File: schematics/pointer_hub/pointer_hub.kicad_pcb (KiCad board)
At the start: 2 copper layers, 34 parts, among them J3 Conn_02x25_Counter_Clockwise, U1 74HC193, U10 74HC245, U11 74HC193, U12 74HC193, U13 74HC193, U14 74HC193, U2 74HC193, U3 74HC193, U4 74HC245, U5 74HC193, U6 74HC245, U7 74HC00, U8 74HC245, U9 74HC00

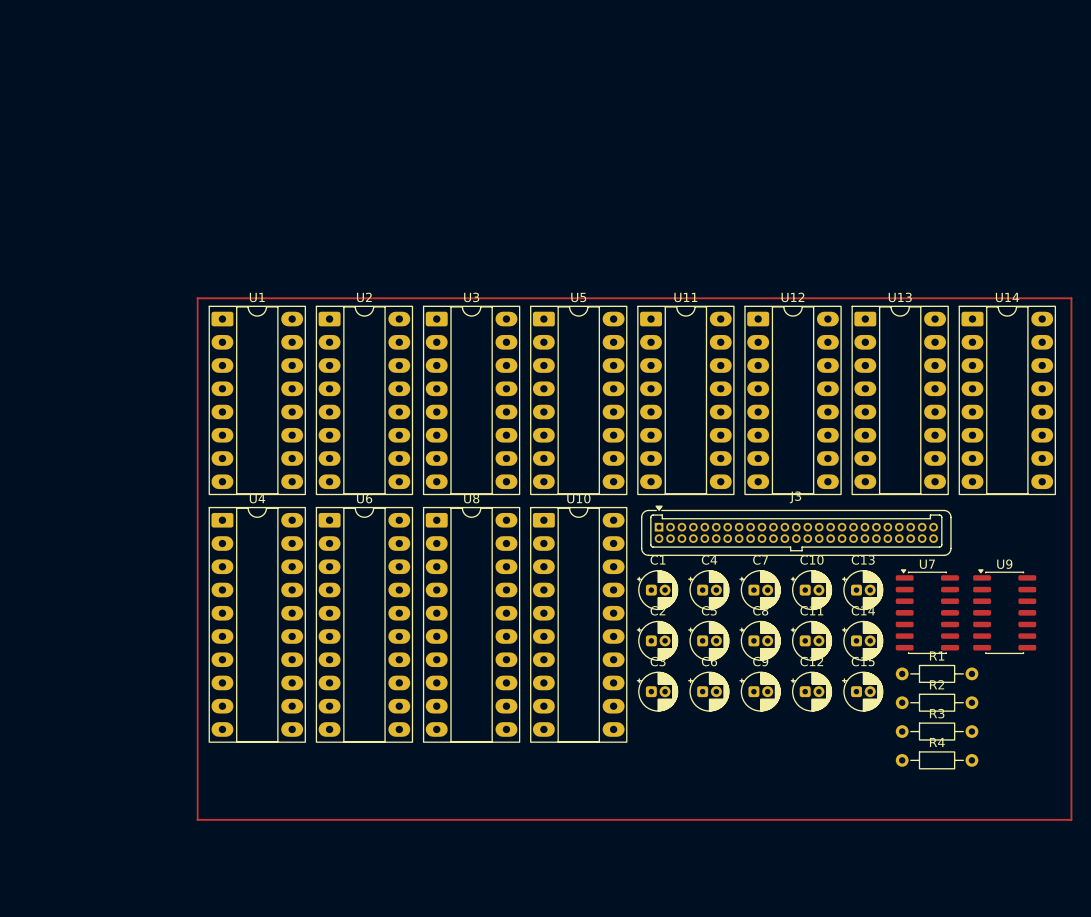
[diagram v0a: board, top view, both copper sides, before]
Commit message: added lowarg to pointerhub, also replaced resistor + vcc logic by grnd and changing A and B pins(A was in became out...)
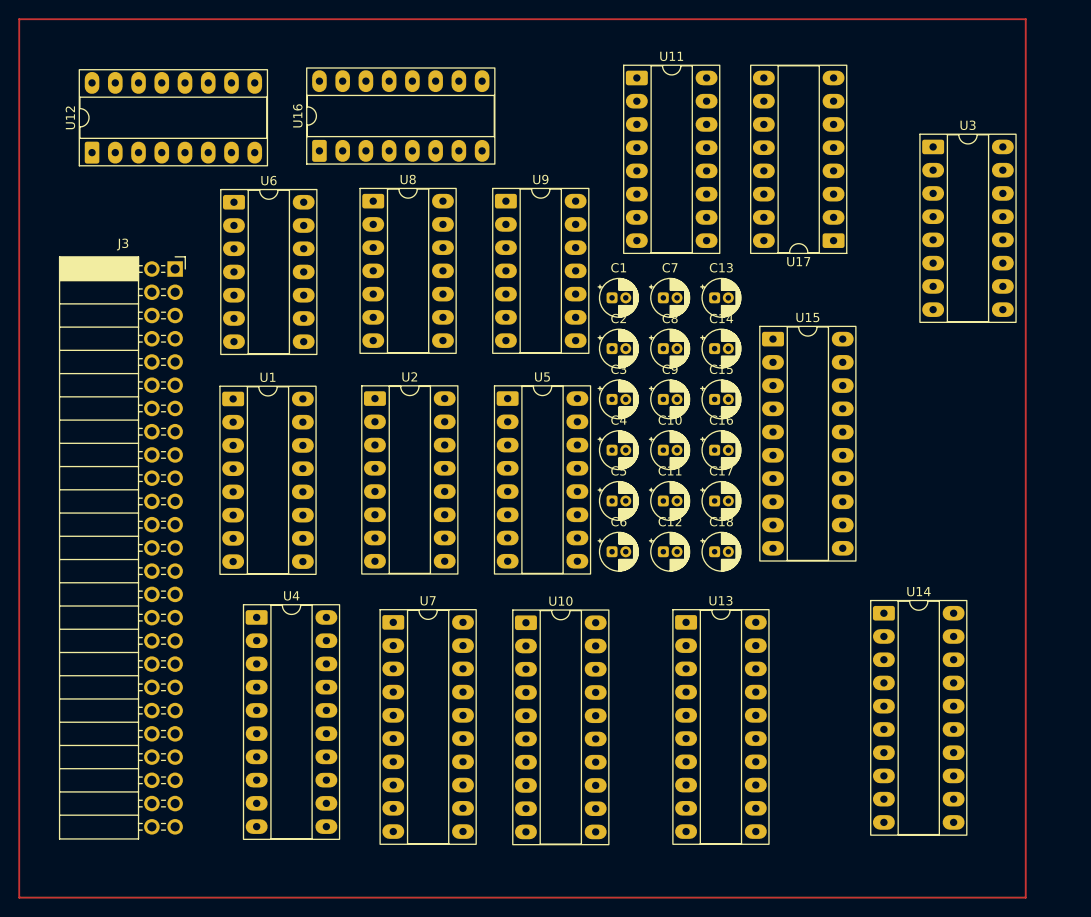
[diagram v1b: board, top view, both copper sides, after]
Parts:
- removed R1, R2, R3, R4: R, Resistor_THT:R_Axial_DIN0204_L3.6mm_D1.6mm_P7.62mm_Horizontal
- added C16: C, Capacitor_THT:CP_Radial_D4.0mm_P1.50mm, F.Cu at (149.5, 86.6)
- added C17: C, Capacitor_THT:CP_Radial_D4.0mm_P1.50mm, F.Cu at (149.5, 92.2)
- added C18: C, Capacitor_THT:CP_Radial_D4.0mm_P1.50mm, F.Cu at (149.5, 97.7)
- added U15: 74LS245, Package_DIP:DIP-20_W7.62mm_Socket_LongPads, F.Cu at (155.9, 74.5)
- added U16: 74LS193, Package_DIP:DIP-16_W7.62mm_Socket_LongPads, F.Cu at (106.3, 53.9)
- added U17: 74LS193, Package_DIP:DIP-16_W7.62mm_Socket_LongPads, F.Cu at (162.5, 63.7)
- J3: footprint Connector_Harwin:Harwin_Gecko-G125-FVX5005L0X_2x25_P1.25mm_Vertical -> Connector_PinSocket_2.54mm:PinSocket_2x25_P2.54mm_Horizontal
- U1, U11, U12, U2, U3, U5: value 74HC193 -> 74LS193
- U10, U4: value 74HC245 -> 74LS245
- U13, U14: value 74HC193 -> 74LS245; footprint Package_DIP:DIP-16_W7.62mm_Socket_LongPads -> Package_DIP:DIP-20_W7.62mm_Socket_LongPads
- U6, U8: value 74HC245 -> 74LS00; footprint Package_DIP:DIP-20_W7.62mm_Socket_LongPads -> Package_DIP:DIP-14_W7.62mm_Socket_LongPads
- U7: value 74HC00 -> 74LS574; footprint Package_SO:SOIC-14_3.9x8.7mm_P1.27mm -> Package_DIP:DIP-20_W7.62mm_Socket_LongPads
- U9: value 74HC00 -> 74LS08; footprint Package_SO:SOIC-14_3.9x8.7mm_P1.27mm -> Package_DIP:DIP-14_W7.62mm_Socket_LongPads
- moved U12 75.0 mm to (81.5, 54.1), turned to 90 degrees
- moved U9 70.7 mm to (126.7, 59.4)
- moved J3 59.9 mm to (90.5, 66.8)
- moved U7 58.4 mm to (114.4, 105.4)
- moved U3 57.4 mm to (173.4, 53.5)
- moved U13 38.5 mm to (146.4, 105.4)
- moved U6 36.3 mm to (97.0, 59.5)
- moved U8 35.6 mm to (112.2, 59.4)
- moved C13 35.5 mm to (149.5, 70.0)
- moved C14 35.5 mm to (149.5, 75.5)
- moved C15 35.5 mm to (149.5, 81.0)
- moved U14 33.6 mm to (168.0, 104.4)
- moved C7 33.4 mm to (143.9, 70.0)
- moved C8 33.4 mm to (143.9, 75.5)
- moved C9 33.4 mm to (143.9, 81.0)
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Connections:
- C1 pad 1: +5V -> GND
- C1 pad 2: GND -> VCC
- C10 pad 1: +5V -> GND
- C10 pad 2: GND -> VCC
- C11 pad 1: +5V -> GND
- C11 pad 2: GND -> VCC
- C12 pad 1: +5V -> GND
- C12 pad 2: GND -> VCC
- C13 pad 1: +5V -> GND
- C13 pad 2: GND -> VCC
- C14 pad 1: +5V -> GND
- C14 pad 2: GND -> VCC
- C15 pad 2: +5V -> VCC
- C2 pad 1: +5V -> GND
- C2 pad 2: GND -> VCC
- C3 pad 1: +5V -> GND
- C3 pad 2: GND -> VCC
- C4 pad 1: +5V -> GND
- C4 pad 2: GND -> VCC
- C5 pad 1: +5V -> VCC
- C6 pad 1: +5V -> VCC
- C7 pad 1: +5V -> GND
- C7 pad 2: GND -> VCC
- C8 pad 1: +5V -> VCC
- C9 pad 1: +5V -> GND
- C9 pad 2: GND -> VCC
- J3 pad 1: GND -> VCC
- J3 pad 10: /BUS6 -> unconnected-(J3-Pin_10-Pad10)
- J3 pad 11: /BUS7 -> /BUS0
- J3 pad 12: /SPReset -> /BUS1
- J3 pad 13: /SPInc -> /BUS2
- J3 pad 14: /SPDec -> /BUS3
- J3 pad 15: /SPHighIn -> /BUS4
- J3 pad 16: /SPLowIn -> /BUS5
- J3 pad 17: /~SPLowOut -> /BUS6
- J3 pad 18: /~SPHighOut -> /BUS7
- J3 pad 19: unconnected-(J3-Pin_19-Pad19) -> GND
- J3 pad 2: /CLK -> GND
- J3 pad 25: unconnected-(J3-Pin_25-Pad25) -> VCC
- J3 pad 26: unconnected-(J3-Pin_26-Pad26) -> VCC
- J3 pad 3: GND -> /~{Clk}
- J3 pad 33: /~PСHighOut -> /~{PСHighOut}
- J3 pad 34: /~PСLowOut -> /~{PСLowOut}
- J3 pad 39: /PCReset -> /Reset
- J3 pad 4: /BUS0 -> /Clk
- J3 pad 40: unconnected-(J3-Pin_40-Pad40) -> /SPInc
- J3 pad 41: unconnected-(J3-Pin_41-Pad41) -> /SPDec
- J3 pad 42: unconnected-(J3-Pin_42-Pad42) -> /SPHighIn
- J3 pad 43: unconnected-(J3-Pin_43-Pad43) -> /SPLowIn
- J3 pad 44: unconnected-(J3-Pin_44-Pad44) -> /~{SPLowOut}
- J3 pad 45: unconnected-(J3-Pin_45-Pad45) -> /~{SPHighOut}
- J3 pad 47: /PULSE -> unconnected-(J3-Pin_47-Pad47)
- J3 pad 48: GND -> /PULSE
- J3 pad 49: /~CLK -> GND
- J3 pad 5: /BUS1 -> /LFromD
- J3 pad 50: GND -> VCC
- J3 pad 6: /BUS2 -> /~{LToD}
- J3 pad 7: /BUS3 -> unconnected-(J3-Pin_7-Pad7)
- J3 pad 8: /BUS4 -> unconnected-(J3-Pin_8-Pad8)
- J3 pad 9: /BUS5 -> unconnected-(J3-Pin_9-Pad9)
- U1 pad 1: /BUS1 -> /BUS5
- U1 pad 10: /BUS2 -> /BUS6
- U1 pad 11: /Pl_A -> /Ph_B
- U1 pad 14: /PCReset -> /Reset
- U1 pad 15: /BUS0 -> /BUS4
- U1 pad 16: +5V -> VCC
- U1 pad 2: /DL_A1 -> /DH_B5
- U1 pad 3: /DL_A0 -> /DH_B4
- U1 pad 6: /DL_A2 -> /DH_B6
- U1 pad 7: /DL_A3 -> /DH_B7
- U1 pad 9: /BUS3 -> /BUS7
- U10 pad 1: Net-(U10-A->B) -> GND
- U10 pad 11: /BUS7 -> /DH_B7
- U10 pad 12: /BUS6 -> /DH_B6
- U10 pad 13: /BUS5 -> /DH_B5
- U10 pad 14: /BUS4 -> /DH_B4
- U10 pad 15: /BUS3 -> /DH_B3
- U10 pad 16: /BUS2 -> /DH_B2
- U10 pad 17: /BUS1 -> /DH_B1
- U10 pad 18: /BUS0 -> /DH_B0
- U10 pad 19: /~SPLowOut -> /~{SPHighOut}
- U10 pad 2: /DL_B0 -> /BUS0
- U10 pad 20: +5V -> VCC
- U10 pad 3: /DL_B1 -> /BUS1
- U10 pad 4: /DL_B2 -> /BUS2
- U10 pad 5: /DL_B3 -> /BUS3
- U10 pad 6: /DL_B4 -> /BUS4
- U10 pad 7: /DL_B5 -> /BUS5
- U10 pad 8: /DL_B6 -> /BUS6
- U10 pad 9: /DL_B7 -> /BUS7
- U11 pad 11: /Ph_B -> /Pl_B
- U11 pad 14: /SPReset -> /Reset
- U11 pad 16: +5V -> VCC
- U11 pad 2: /DH_B5 -> /DL_B5
- U11 pad 3: /DH_B4 -> /DL_B4
- U11 pad 4: Net-(U11-DOWN) -> /CPd_B
- U11 pad 5: Net-(U11-UP) -> /CPu_B
- U11 pad 6: /DH_B6 -> /DL_B6
- U11 pad 7: /DH_B7 -> /DL_B7
- U12 pad 11: /Ph_B -> /Pl_B
- U12 pad 12: unconnected-(U12-~{CO}-Pad12) -> Net-(U1-UP)
- U12 pad 13: unconnected-(U12-~{BO}-Pad13) -> Net-(U1-DOWN)
- U12 pad 14: /SPReset -> /Reset
- U12 pad 16: +5V -> VCC
- U12 pad 2: /DH_B1 -> /DL_B1
- U12 pad 3: /DH_B0 -> /DL_B0
- U12 pad 6: /DH_B2 -> /DL_B2
- U12 pad 7: /DH_B3 -> /DL_B3
- U13 pad 1: /BUS5 -> GND
- U13 pad 10: /BUS6 -> GND
- U13 pad 11: /Pl_B -> Net-(U13-B7)
- U13 pad 12: Net-(U13-~{CO}) -> Net-(U13-B6)
- U13 pad 13: Net-(U13-~{BO}) -> Net-(U13-B5)
- U13 pad 14: /SPReset -> Net-(U13-B4)
- U13 pad 15: /BUS4 -> Net-(U13-B3)
- U13 pad 16: +5V -> Net-(U13-B2)
- U13 pad 2: /DL_B5 -> /BUS0
- U13 pad 3: /DL_B4 -> /BUS1
- U13 pad 4: /CPd_B -> /BUS2
- U13 pad 5: /CPu_B -> /BUS3
- U13 pad 6: /DL_B6 -> /BUS4
- U13 pad 7: /DL_B7 -> /BUS5
- U13 pad 8: GND -> /BUS6
- U14 pad 1: /BUS1 -> GND
- U14 pad 10: /BUS2 -> GND
- U14 pad 11: /Pl_B -> /DL_A7
- U14 pad 12: Net-(U11-UP) -> /DL_A6
- U14 pad 13: Net-(U11-DOWN) -> /DL_A5
- U14 pad 14: /SPReset -> /DL_A4
- U14 pad 15: /BUS0 -> /DL_A3
- U14 pad 16: +5V -> /DL_A2
- U14 pad 2: /DL_B1 -> /BUS0
- U14 pad 3: /DL_B0 -> /BUS1
- U14 pad 4: Net-(U13-~{BO}) -> /BUS2
- U14 pad 5: Net-(U13-~{CO}) -> /BUS3
- U14 pad 6: /DL_B2 -> /BUS4
- U14 pad 7: /DL_B3 -> /BUS5
- U14 pad 8: GND -> /BUS6
- U14 pad 9: /BUS3 -> /BUS7
- U2 pad 1: /BUS5 -> /BUS1
- U2 pad 10: /BUS6 -> /BUS2
- U2 pad 12: Net-(U2-~{CO}) -> unconnected-(U2-~{CO}-Pad12)
- U2 pad 13: Net-(U2-~{BO}) -> unconnected-(U2-~{BO}-Pad13)
- U2 pad 14: /PCReset -> /Reset
- U2 pad 15: /BUS4 -> /BUS0
- U2 pad 16: +5V -> VCC
- U2 pad 2: /DH_A5 -> /DH_A1
- U2 pad 3: /DH_A4 -> /DH_A0
- U2 pad 4: Net-(U1-~{BO}) -> Net-(U16-~{BO})
- U2 pad 5: Net-(U1-~{CO}) -> Net-(U16-~{CO})
- U2 pad 6: /DH_A6 -> /DH_A2
- U2 pad 7: /DH_A7 -> /DH_A3
- U2 pad 9: /BUS7 -> /BUS3
- U3 pad 11: /Ph_A -> /Pl_A
- U3 pad 12: unconnected-(U3-~{CO}-Pad12) -> Net-(U16-UP)
- U3 pad 13: unconnected-(U3-~{BO}-Pad13) -> Net-(U16-DOWN)
- U3 pad 14: /PCReset -> /Reset
- U3 pad 16: +5V -> VCC
- U3 pad 2: /DH_A1 -> /DL_A1
- U3 pad 3: /DH_A0 -> /DL_A0
- U3 pad 4: Net-(U2-~{BO}) -> Net-(U17-~{BO})
- U3 pad 5: Net-(U2-~{CO}) -> Net-(U17-~{CO})
- U3 pad 6: /DH_A2 -> /DL_A2
- U3 pad 7: /DH_A3 -> /DL_A3
- U4 pad 1: Net-(U4-A->B) -> GND
- U4 pad 11: /BUS7 -> /DL_B7
- U4 pad 12: /BUS6 -> /DL_B6
- U4 pad 13: /BUS5 -> /DL_B5
- U4 pad 14: /BUS4 -> /DL_B4
- U4 pad 15: /BUS3 -> /DL_B3
- U4 pad 16: /BUS2 -> /DL_B2
- U4 pad 17: /BUS1 -> /DL_B1
- U4 pad 18: /BUS0 -> /DL_B0
- U4 pad 19: /~PСHighOut -> /~{SPLowOut}
- U4 pad 2: /DH_A0 -> /BUS0
- U4 pad 20: +5V -> VCC
- U4 pad 3: /DH_A1 -> /BUS1
- U4 pad 4: /DH_A2 -> /BUS2
- U4 pad 5: /DH_A3 -> /BUS3
- U4 pad 6: /DH_A4 -> /BUS4
- U4 pad 7: /DH_A5 -> /BUS5
- U4 pad 8: /DH_A6 -> /BUS6
- U4 pad 9: /DH_A7 -> /BUS7
- U5 pad 1: /BUS5 -> /BUS1
- U5 pad 10: /BUS6 -> /BUS2
- U5 pad 11: /Pl_A -> /Ph_B
- U5 pad 12: Net-(U1-UP) -> unconnected-(U5-~{CO}-Pad12)
- U5 pad 13: Net-(U1-DOWN) -> unconnected-(U5-~{BO}-Pad13)
- U5 pad 14: /PCReset -> /Reset
- U5 pad 15: /BUS4 -> /BUS0
- U5 pad 16: +5V -> VCC
- U5 pad 2: /DL_A5 -> /DH_B1
- U5 pad 3: /DL_A4 -> /DH_B0
- U5 pad 4: /CPd_A -> Net-(U1-~{BO})
- U5 pad 5: /CPu_A -> Net-(U1-~{CO})
- U5 pad 6: /DL_A6 -> /DH_B2
- U5 pad 7: /DL_A7 -> /DH_B3
- U5 pad 9: /BUS7 -> /BUS3
- U6 pad 1: Net-(U6-A->B) -> /~{Clk}
- U6 pad 10: GND -> /PCHighIn
- U6 pad 11: /BUS7 -> /Pl_A
- U6 pad 12: /BUS6 -> /PULSE
- U6 pad 13: /BUS5 -> /PCLowIn
- U6 pad 14: /BUS4 -> VCC
- U6 pad 2: /DL_A0 -> /PCInc
- U6 pad 3: /DL_A1 -> /CPu_A
- U6 pad 4: /DL_A2 -> /~{Clk}
- U6 pad 5: /DL_A3 -> /PCDec
- U6 pad 6: /DL_A4 -> /CPd_A
- U6 pad 7: /DL_A5 -> GND
- U6 pad 8: /DL_A6 -> /Ph_A
- U6 pad 9: /DL_A7 -> /PULSE
- U7 pad 1: /SPHighIn -> GND
- U7 pad 10: /~CLK -> GND
- U7 pad 11: /CPd_B -> Net-(U7-Cp)
- U7 pad 12: /SPDec -> Net-(U13-B7)
- U7 pad 13: /~CLK -> Net-(U13-B6)
- U7 pad 14: +5V -> Net-(U13-B5)
- U7 pad 2: /PULSE -> /BUS0
- U7 pad 3: /Ph_B -> /BUS1
- U7 pad 4: /SPLowIn -> /BUS2
- U7 pad 5: /PULSE -> /BUS3
- U7 pad 6: /Pl_B -> /BUS4
- U7 pad 7: GND -> /BUS5
- U7 pad 8: /CPu_B -> /BUS6
- U7 pad 9: /SPInc -> /BUS7
- U8 pad 1: Net-(U8-A->B) -> /SPLowIn
- U8 pad 10: GND -> /~{Clk}
- U8 pad 11: /BUS7 -> /CPu_B
- U8 pad 12: /BUS6 -> /SPInc
- U8 pad 13: /BUS5 -> /~{Clk}
- U8 pad 14: /BUS4 -> VCC
- U8 pad 2: /DH_B0 -> /PULSE
- U8 pad 3: /DH_B1 -> /Pl_B
- U8 pad 4: /DH_B2 -> /SPHighIn
- U8 pad 5: /DH_B3 -> /PULSE
- U8 pad 6: /DH_B4 -> /Ph_B
- U8 pad 7: /DH_B5 -> GND
- U8 pad 8: /DH_B6 -> /CPd_B
- U8 pad 9: /DH_B7 -> /SPDec
- U9 pad 1: /PULSE -> /LFromD
- U9 pad 10: /PCInc -> unconnected-(U9-Pad10)
- U9 pad 11: /CPd_A -> unconnected-(U9-Pad11)
- U9 pad 12: /~CLK -> unconnected-(U9-Pad12)
- U9 pad 13: /PCDec -> unconnected-(U9-Pad13)
- U9 pad 14: +5V -> VCC
- U9 pad 2: /PCHighIn -> /Clk
- U9 pad 3: /Ph_A -> Net-(U7-Cp)
- U9 pad 4: /PULSE -> unconnected-(U9-Pad4)
- U9 pad 5: /PCLowIn -> unconnected-(U9-Pad5)
- U9 pad 6: /Pl_A -> unconnected-(U9-Pad6)
- U9 pad 8: /CPu_A -> unconnected-(U9-Pad8)
- U9 pad 9: /~CLK -> unconnected-(U9-Pad9)
